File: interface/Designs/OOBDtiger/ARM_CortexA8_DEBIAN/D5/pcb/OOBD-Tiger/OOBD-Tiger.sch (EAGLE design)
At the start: 122 parts, among them IC1 ADM3053M, IC2 ADM3053M, IC4 DS3231, U1 SY6280, U10 MP1482DS, U2 SN65HVD230(SO8), U3 SY6280, U6 SN65HVD230(SO8)

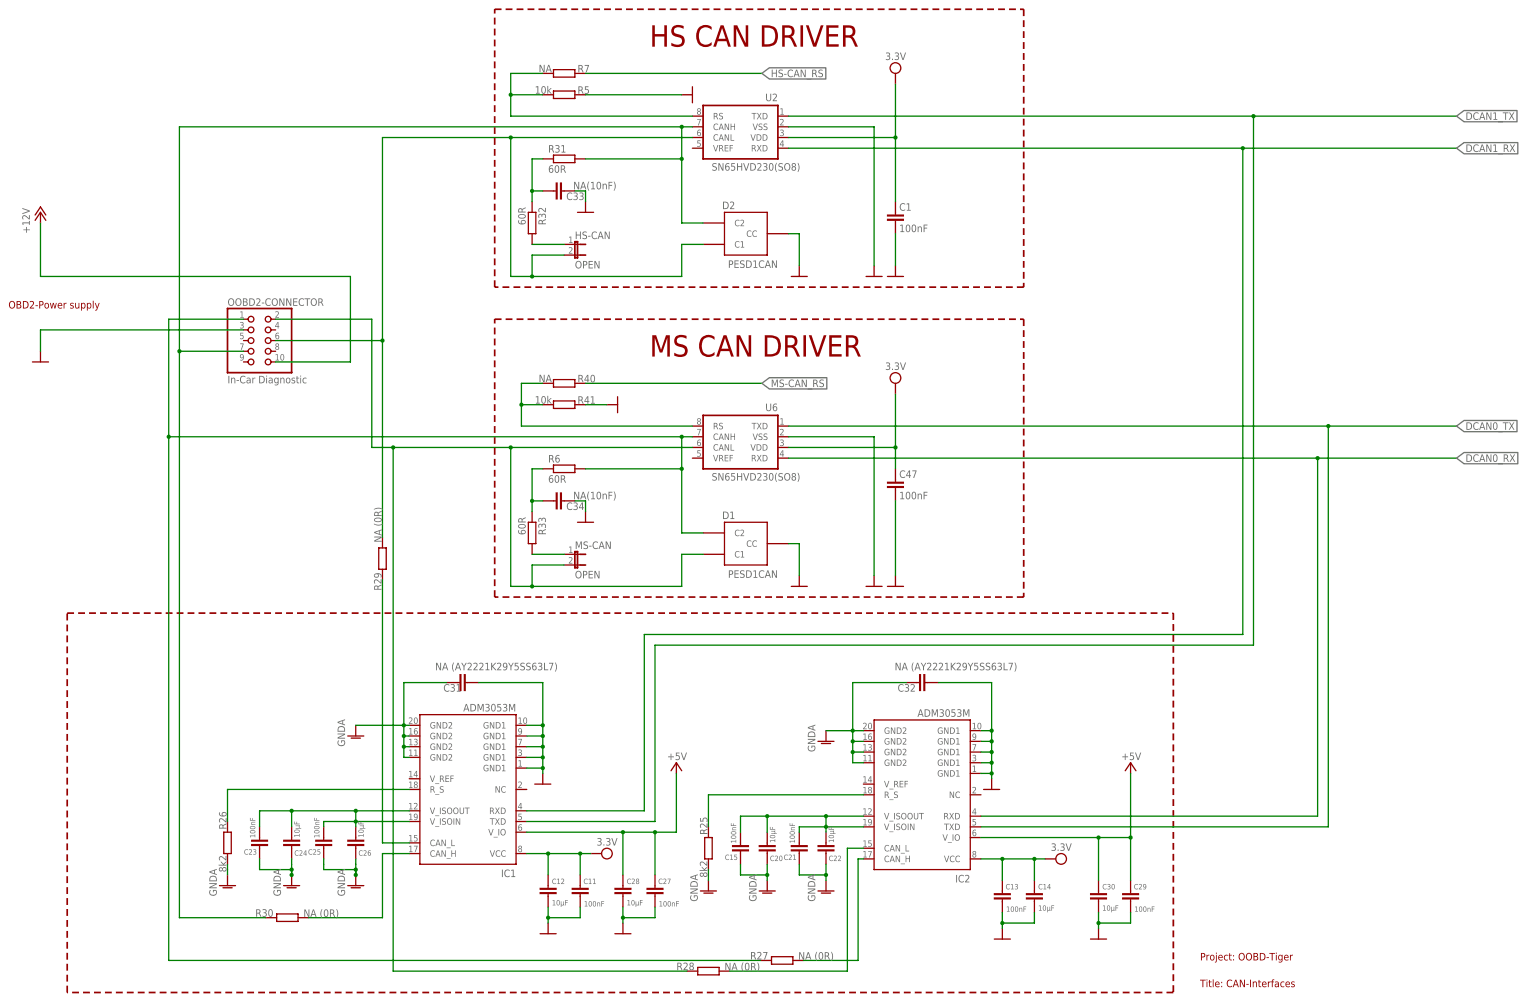
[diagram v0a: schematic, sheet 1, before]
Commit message: minor changes on CAN interfaces and start component placing improvement
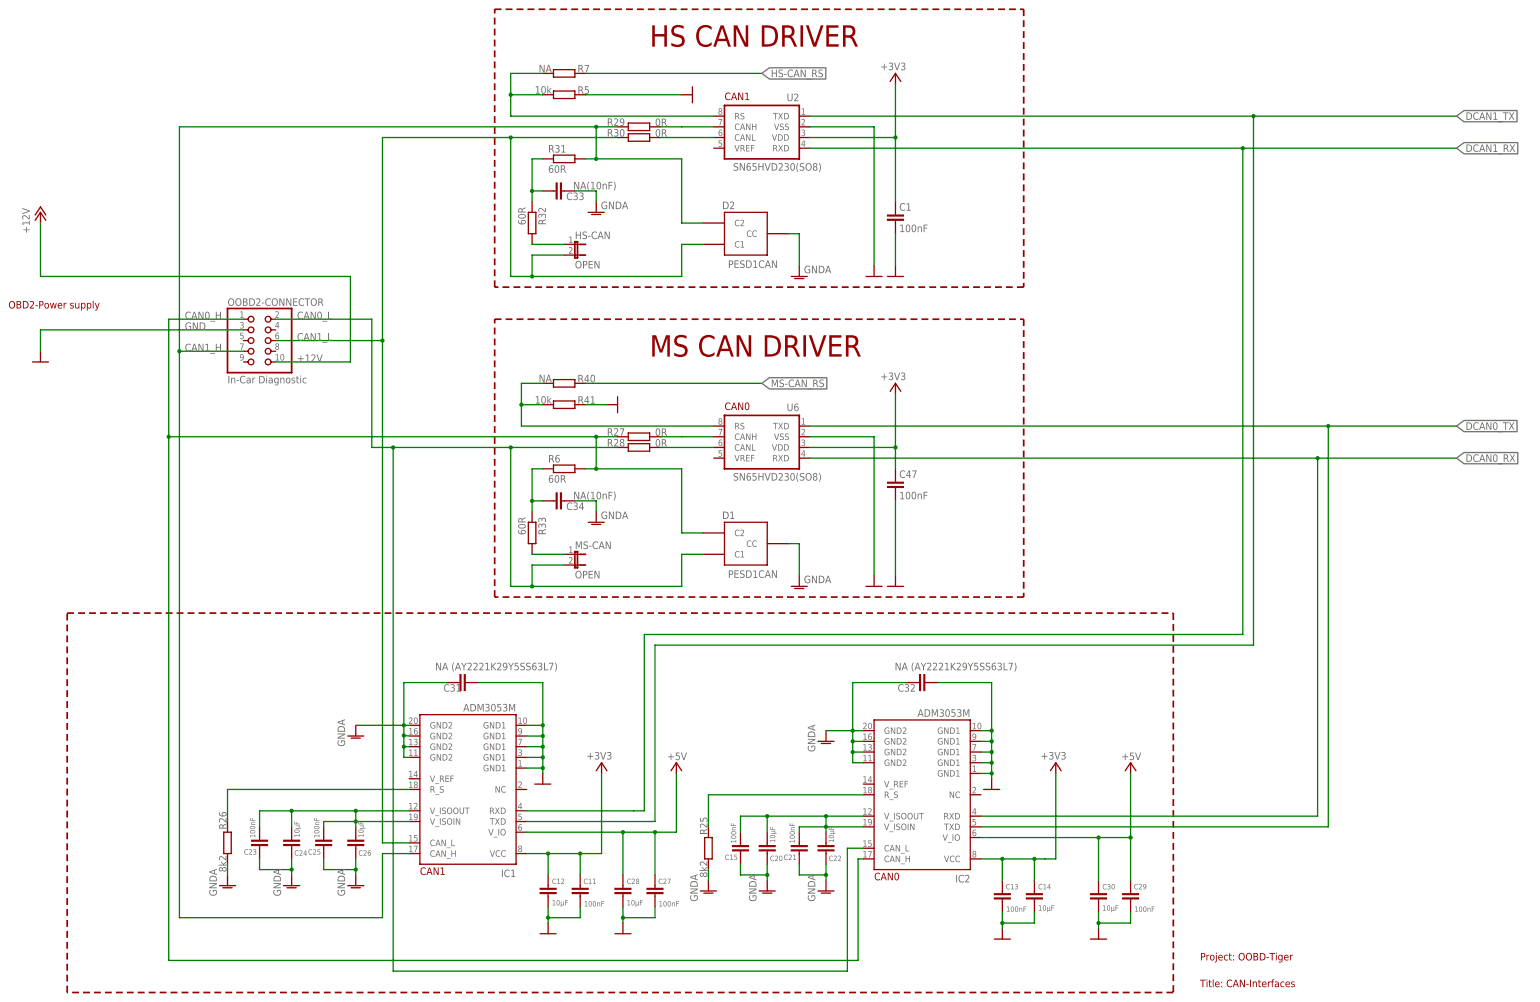
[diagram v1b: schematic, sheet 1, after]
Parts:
- R27, R28, R29, R30: value NA (0R) -> 0R
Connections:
- removed net N$12: IC2.CAN_H, R27.2
- removed net N$34: IC2.CAN_L, R28.2
- removed net N$35: IC1.CAN_H, R30.2
- removed net N$36: IC1.CAN_L, R29.1
- removed net N$37: IC1.TXD
- removed net N$38: IC1.RXD
- new net N$40: R27.2, U6.CANH
- new net N$41: R30.2, U2.CANL
- new net N$42: R28.2, U6.CANL
- new net N$45: R29.1, U2.CANH
- net +3V3: now also C1.1, C11.1, C12.1, C13.1, C14.1, C47.1, IC1.VCC, IC2.VCC, R47.2, U2.VDD, U6.VDD
- net 3V3: no longer C1.1, C11.1, C12.1, C13.1, C14.1, C47.1, IC1.VCC, IC2.VCC, R47.2, U2.VDD, U6.VDD
- net CAN0_H: now also IC2.CAN_H; no longer U6.CANH
- net CAN0_L: now also IC2.CAN_L; no longer U6.CANL
- net CAN1_H: now also IC1.CAN_H, R29.2; no longer R30.1, U2.CANH
- net CAN1_L: now also IC1.CAN_L, R30.1; no longer R29.2, U2.CANL
- net DCAN1_RX: now also IC1.RXD
- net DCAN1_TX: now also IC1.TXD
- net GND: no longer C33.2, C34.2, D1.CC, D2.CC
- net GNDA: now also C33.2, C34.2, D1.CC, D2.CC
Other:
- note added: "CAN0"
- note added: "CAN1"
- moved on the sheet: R27, R28, R29, R30, U2, U6

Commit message: further improvement on component placing (94,2% autotrouter) now!
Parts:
- C14: device rcl:C-EUC0603 -> rcl:C-EUC0805K
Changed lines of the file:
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@@
 <setting verticaltext="up"/>
 </settings>
-<grid distance="50" unitdist="mil" unit="mil" style="lines" multiple="1" display="yes" altdistance="0.01" altunitdist="inch" altunit="inch"/>
+<grid distance="0.1" unitdist="inch" unit="inch" style="lines" multiple="1" display="no" altdistance="0.01" altunitdist="inch" altunit="inch"/>
 <layers>
 <layer number="1" name="Top" color="4" fill="1" visible="no" active="no"/>
@@
 <part name="C12" library="rcl" deviceset="C-EU" device="C0805K" value="10µF"/>
 <part name="C13" library="rcl" deviceset="C-EU" device="C0603K" value="100nF"/>
-<part name="C14" library="rcl" deviceset="C-EU" device="C0603" value="10µF"/>
 <part name="C15" library="rcl" deviceset="C-EU" device="C0603K" value="100nF"/>
 <part name="C20" library="rcl" deviceset="C-EU" device="C0805K" value="10µF"/>
@@
 <part name="+3V10" library="supply1" deviceset="+3V3" device=""/>
 <part name="+3V11" library="supply1" deviceset="+3V3" device=""/>
+<part name="C14" library="rcl" deviceset="C-EU" device="C0805K" value="10µF"/>
 </parts>
 <sheets>
@@
 <attribute name="VALUE" x="244.729" y="31.877" size="1.27" layer="96"/>
 </instance>
-<instance part="C14" gate="G$1" x="251.46" y="36.83" smashed="yes">
-<attribute name="NAME" x="252.349" y="37.211" size="1.27" layer="95"/>
-<attribute name="VALUE" x="252.349" y="32.131" size="1.27" layer="96"/>
-</instance>
 <instance part="C15" gate="G$1" x="181.61" y="48.26" smashed="yes">
 <attribute name="NAME" x="180.975" y="45.466" size="1.27" layer="95" rot="R180"/>
@@
 <instance part="+3V11" gate="G$1" x="148.59" y="67.31" smashed="yes">
 <attribute name="VALUE" x="151.13" y="69.85" size="1.778" layer="96" rot="R180"/>
+</instance>
+<instance part="C14" gate="G$1" x="251.46" y="36.83" smashed="yes">
+<attribute name="NAME" x="252.349" y="37.211" size="1.27" layer="95"/>
+<attribute name="VALUE" x="252.349" y="32.131" size="1.27" layer="96"/>
 </instance>
 </instances>
@@
 <pinref part="GND47" gate="1" pin="GND"/>
 <wire x1="243.84" y1="31.75" x2="243.84" y2="29.21" width="0.1524" layer="91"/>
-<pinref part="C14" gate="G$1" pin="2"/>
 <wire x1="243.84" y1="29.21" x2="243.84" y2="27.94" width="0.1524" layer="91"/>
 <wire x1="251.46" y1="31.75" x2="251.46" y2="29.21" width="0.1524" layer="91"/>
 <wire x1="243.84" y1="29.21" x2="251.46" y2="29.21" width="0.1524" layer="91"/>
 <junction x="243.84" y="29.21"/>
+<pinref part="C14" gate="G$1" pin="2"/>
 </segment>
 <segment>
@@
 <segment>
 <pinref part="IC2" gate="G$1" pin="VCC"/>
-<pinref part="C14" gate="G$1" pin="1"/>
 <wire x1="251.46" y1="44.45" x2="251.46" y2="39.37" width="0.1524" layer="91"/>
 <pinref part="C13" gate="G$1" pin="1"/>
@@
 <wire x1="256.54" y1="44.45" x2="256.54" y2="64.77" width="0.1524" layer="91"/>
 <pinref part="+3V10" gate="G$1" pin="+3V3"/>
-</segment>
-</net>
+<pinref part="C14" gate="G$1" pin="1"/>
+</segment>
+</net>
